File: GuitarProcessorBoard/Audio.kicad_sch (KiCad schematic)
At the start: 47 parts, among them U1 TL074, U2 TL072, U3 TLV320AIC3204

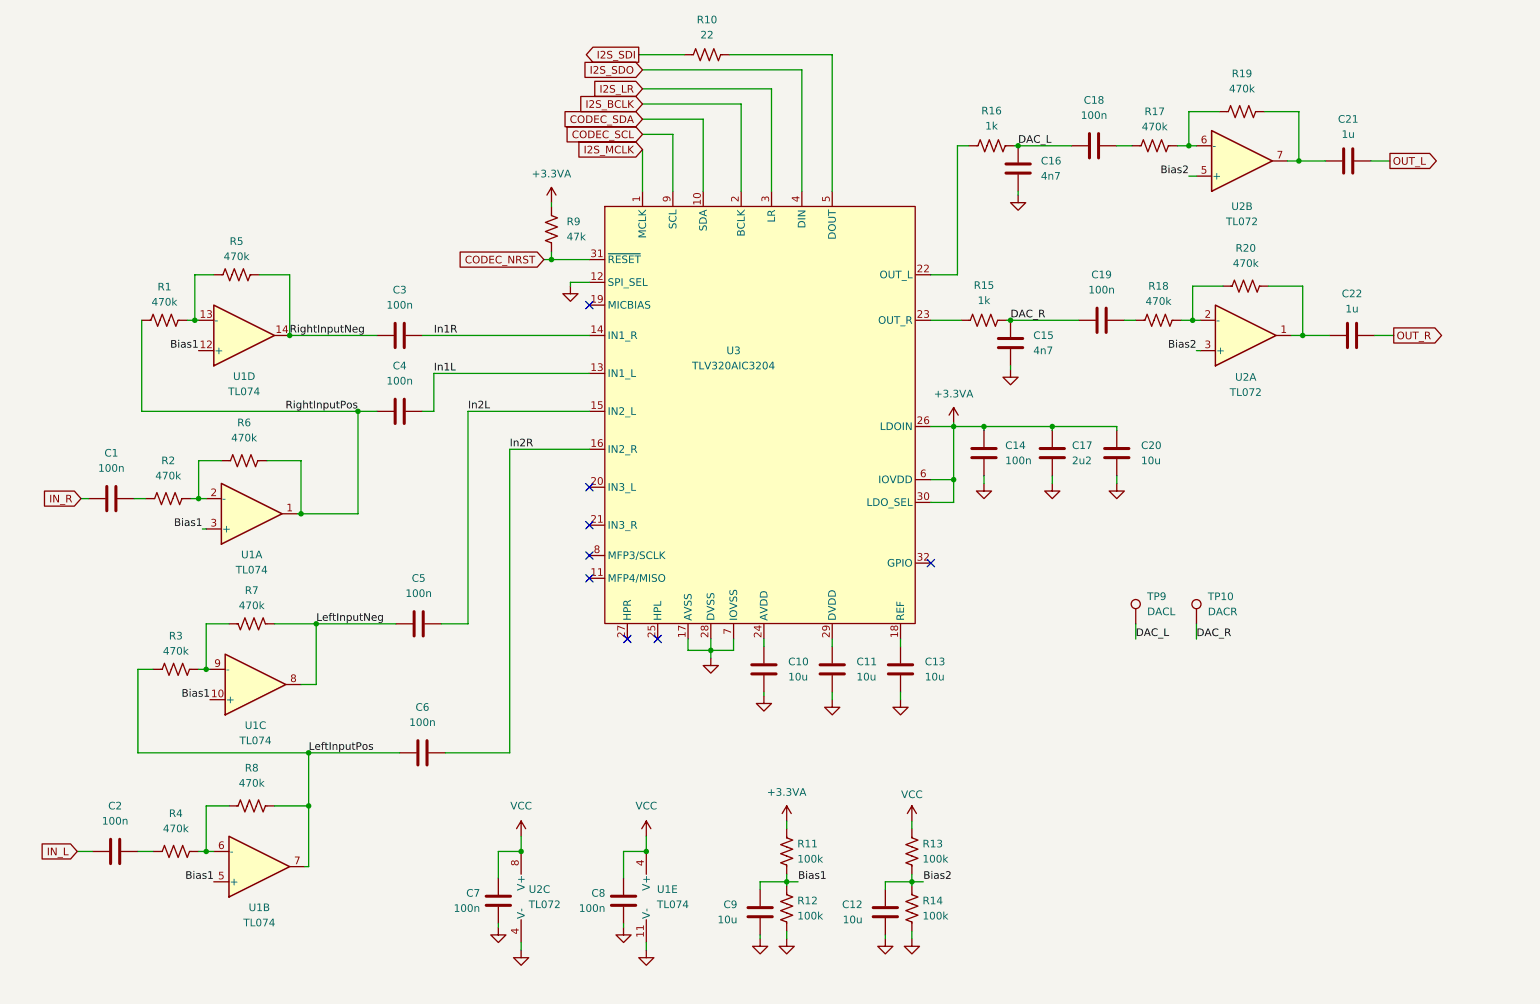
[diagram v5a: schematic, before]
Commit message: input/output opamp stages changed
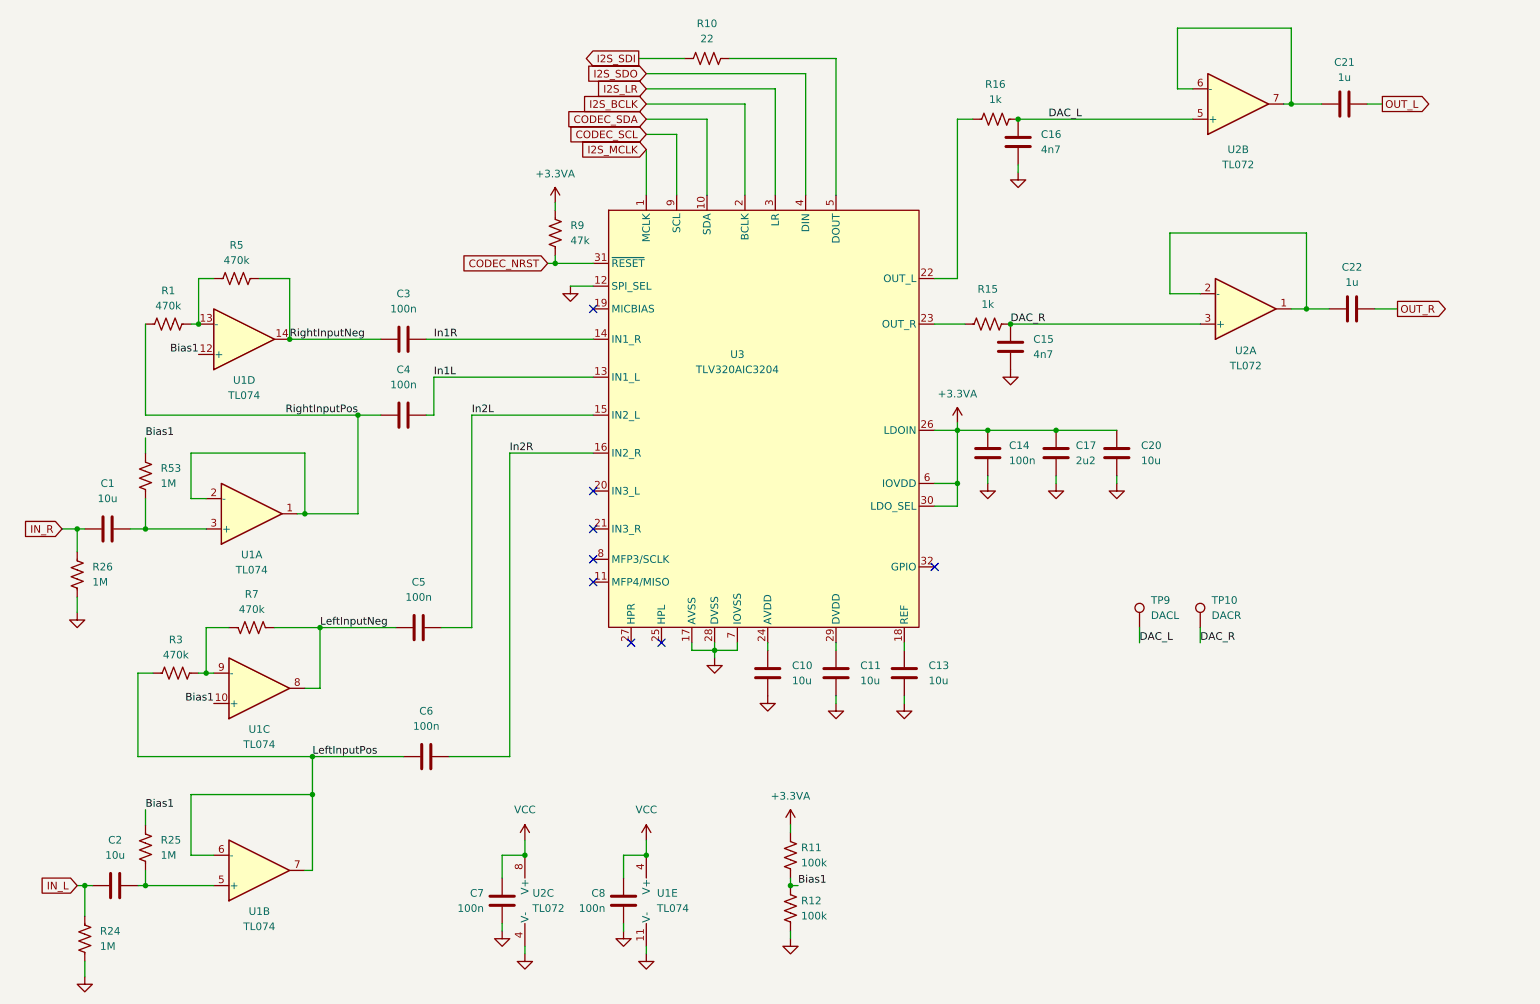
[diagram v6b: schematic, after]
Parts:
- removed C12, C9: 10u, Capacitor_SMD:C_0805_2012Metric, symbol Device:C
- removed C18, C19: 100n, Capacitor_SMD:C_0805_2012Metric, symbol Device:C
- removed R13, R14: 100k, Resistor_SMD:R_0805_2012Metric, symbol Device:R_US
- removed R17, R18, R19, R2, R20, R4, R6, R8: 470k, Resistor_SMD:R_0805_2012Metric, symbol Device:R_US
- added R24, R25, R26, R53: 1M, Resistor_SMD:R_0805_2012Metric, symbol Device:R_US
- C1, C2: value 100n -> 10u
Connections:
- net Bias1: now also R25.1, R53.1; no longer U1.3 (+), U1.5 (+)
- net DAC_L: now also U2.5 (+)
- net DAC_R: now also U2.3 (+)
- net GND: now also R24.2, R26.2
- net IN_L: now also R24.1
- net IN_R: now also R26.1
- net LeftInputPos: now also U1.6 (-)
- net RightInputPos: now also U1.2 (-)
- net at C22.1, U2.1: now also U2.2 (-)
- net at C1.2: now also U1.3 (+), R53.2
- net at C2.2: now also U1.5 (+), R25.2
- net at C21.1, U2.7: now also U2.6 (-)
- removed net Bias2: U2.3 (+), U2.5 (+)
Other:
- moved on the sheet: C1, C10, C11, C13, C14, C15, C16, C17, C2, C21, C22, C3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

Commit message: basic routing, DRC passes
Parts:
- added TP11: CM, TestPoint:TestPoint_THTPad_D2.0mm_Drill1.0mm_VAL, symbol Connector:TestPoint
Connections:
- net Bias1: now also TP11.1
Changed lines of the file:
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@@
 		)
 	)
+	(wire
+		(pts
+			(xy 191.008 130.81) (xy 191.008 133.35)
+		)
+		(stroke
+			(width 0)
+			(type default)
+		)
+	)
 	(label "RightInputNeg"
 		(at 58.42 82.55 0)
@@
 		)
 	)
+	(label "Bias1"
+		(at 191.008 133.35 0)
+		(effects
+			(font
+				(size 1.27 1.27)
+			)
+			(justify left bottom)
+		)
+	)
 	(global_label "IN_R"
 		(shape input)
@@
 					(unit 1)
 				)
+			)
+		)
+	)
+	(symbol
+		(lib_id "Connector:TestPoint")
+		(at 191.008 130.81 0)
+		(unit 1)
+		(body_style 1)
+		(exclude_from_sim no)
+		(in_bom no)
+		(on_board yes)
+		(in_pos_files yes)
+		(dnp no)
+		(fields_autoplaced yes)
+		(property "Reference" "TP11"
+			(at 193.04 126.2379 0)
+			(show_name no)
+			(do_not_autoplace no)
+			(effects
+				(font
+					(size 1.27 1.27)
+				)
+				(justify left)
+			)
+		)
+		(property "Value" "CM"
+			(at 193.04 128.7779 0)
+			(show_name no)
+			(do_not_autoplace no)
+			(effects
+				(font
+					(size 1.27 1.27)
+				)
+				(justify left)
+			)
+		)
+		(property "Footprint" "TestPoint:TestPoint_THTPad_D2.0mm_Drill1.0mm_VAL"
+			(at 196.088 130.81 0)
+			(hide yes)
+			(show_name no)
+			(do_not_autoplace no)
+			(effects
+				(font
+					(size 1.27 1.27)
+				)
+			)
+		)
+		(property "Datasheet" ""
+			(at 196.088 130.81 0)
+			(hide yes)
+			(show_name no)
+			(do_not_autoplace no)
+			(effects
+				(font
+					(size 1.27 1.27)
+				)
+			)
+		)
+		(property "Description" "test point"
+			(at 191.008 130.81 0)
+			(hide yes)
+			(show_name no)
+			(do_not_autoplace no)
+			(effects
+				(font
+					(size 1.27 1.27)
+				)
+			)
+		)
+		(pin "1"
+		)
+		(instances
+			(project "GuitarProcessorBoard"
+				(path "/524c695b-c632-4089-9e9a-ef0f89cad1b2/ef3a9a4a-abe1-4d77-855c-3594c7f88930"
+					(reference "TP11")
+					(unit 1)
+				)

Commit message: Dattorro verb running fast enough woo
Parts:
- C3, C4, C5, C6: value 100n -> 1u
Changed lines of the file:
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@@
 			)
 		)
-		(property "Value" "100n"
+		(property "Value" "1u"
 			(at 77.47 90.17 90)
 			(show_name no)
@@
 		(fields_autoplaced yes)
 		(property "Reference" "R12"
-			(at 144.018 176.5299 0)
+			(at 144.78 176.5299 0)
 			(show_name no)
 			(do_not_autoplace no)
@@
 		)
 		(property "Value" "100k"
-			(at 144.018 179.0699 0)
+			(at 144.78 179.0699 0)
 			(show_name no)
 			(do_not_autoplace no)
@@
 			)
 		)
-		(property "Value" "100n"
+		(property "Value" "1u"
 			(at 81.28 147.32 90)
 			(show_name no)
@@
 			)
 		)
-		(property "Value" "100n"
+		(property "Value" "1u"
 			(at 77.47 77.47 90)
 			(show_name no)
@@
 			)
 		)
-		(property "Value" "100n"
+		(property "Value" "1u"
 			(at 80.01 125.73 90)
 			(show_name no)
